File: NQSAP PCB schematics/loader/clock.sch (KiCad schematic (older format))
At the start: 17 parts, among them SW2 PULSE, SW3 RUN, U5 74HCT04, U6 74HCT08, U7 NE556, U8 74HCT27

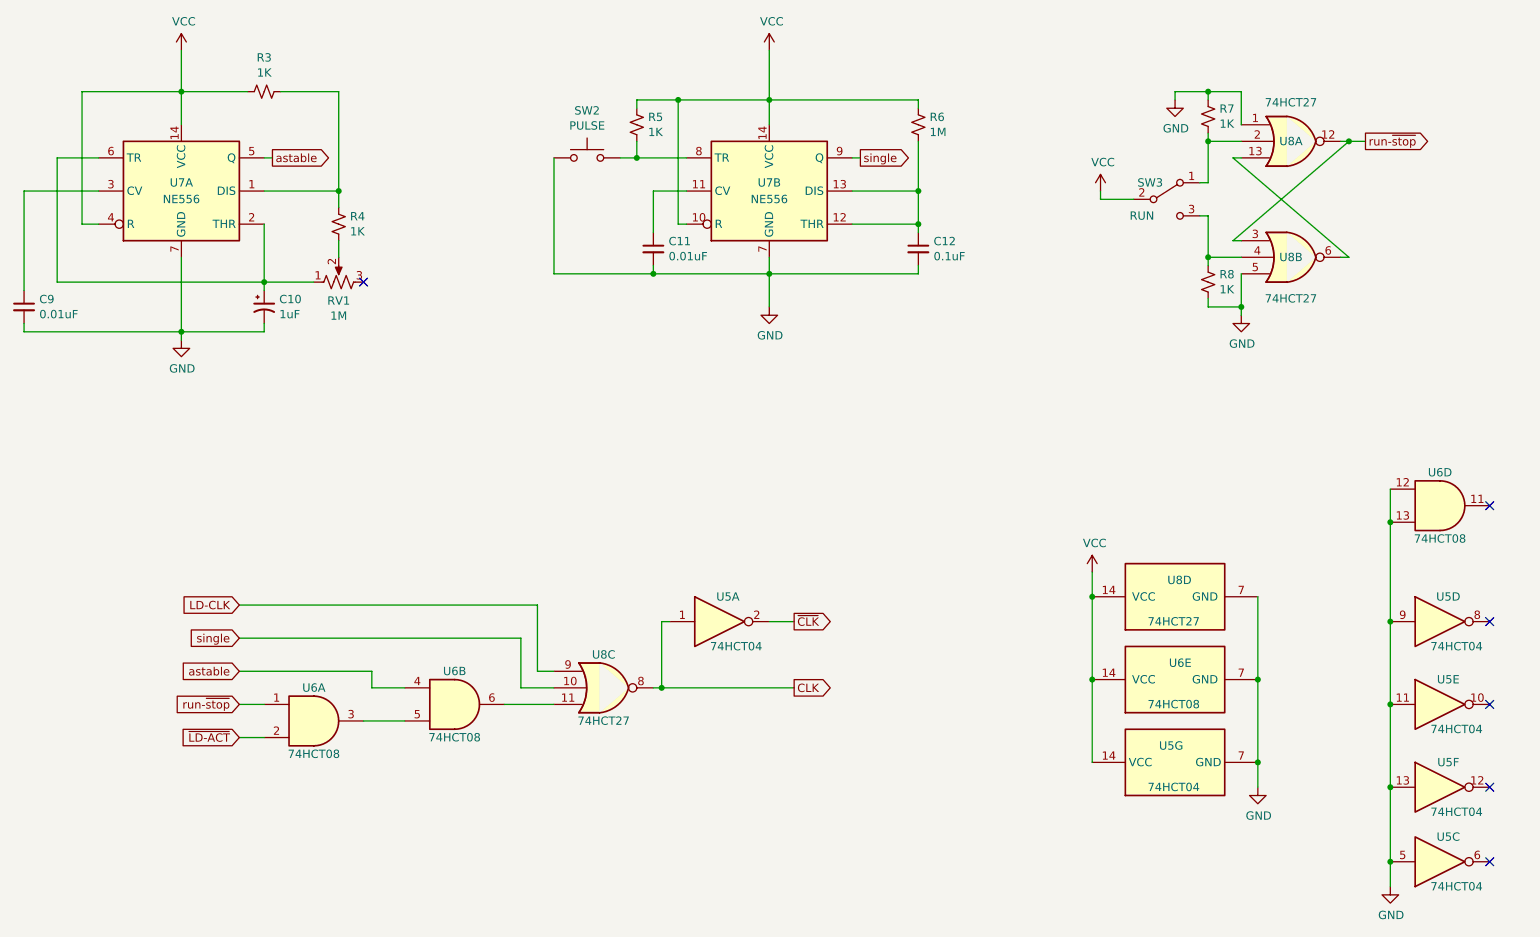
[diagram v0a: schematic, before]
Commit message: Add RAM, update and add gerbers for new boards
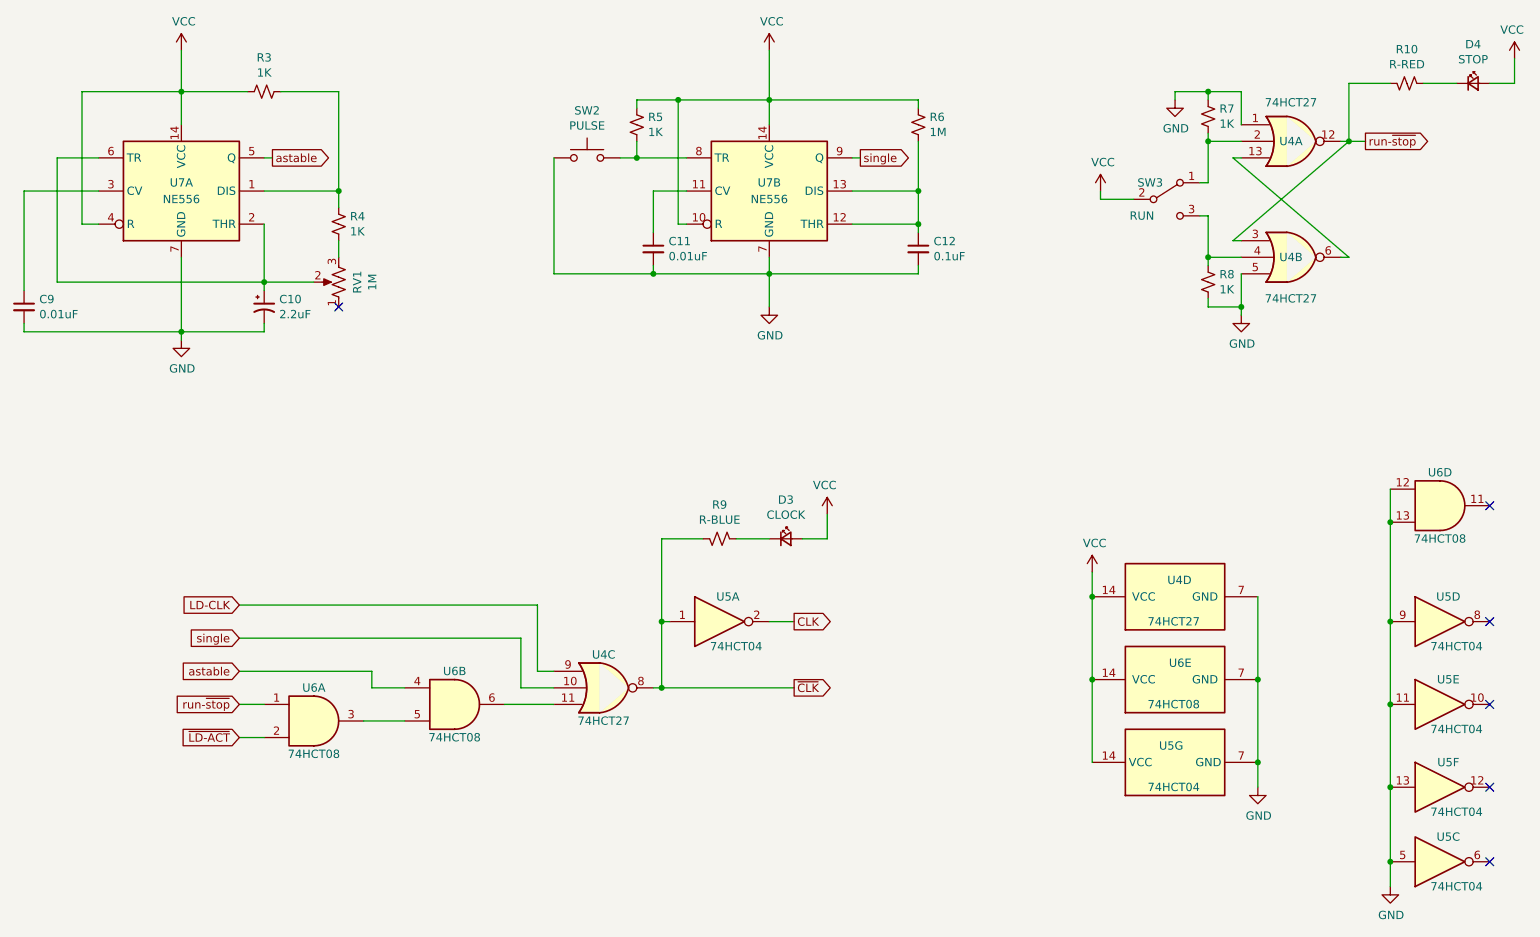
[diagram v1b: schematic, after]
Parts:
- added D3: CLOCK, LED_SMD:LED_0805_2012Metric_Pad1.15x1.40mm_HandSolder, symbol Device:LED_Small
- added D4: STOP, LED_SMD:LED_0805_2012Metric_Pad1.15x1.40mm_HandSolder, symbol Device:LED_Small
- added R10: R-RED, Resistor_SMD:R_0805_2012Metric_Pad1.20x1.40mm_HandSolder, symbol Device:R_Small_US
- added R9: R-BLUE, Resistor_SMD:R_0805_2012Metric_Pad1.20x1.40mm_HandSolder, symbol Device:R_Small_US
- C10: value 1uF -> 2.2uF
- RV1: footprint Potentiometer_THT:Potentiometer_Vishay_T73YP_Vertical -> Potentiometer_THT:Potentiometer_Bourns_3386F_Vertical
- renumbered U8 to U4
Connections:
- net CLK: now also U5.2; no longer U4.8, U5.1
- net VCC: now also D3.2 (A), D4.2 (A)
- net run-~stop: now also R10.1
- net ~CLK: now also U4.8, U5.1, R9.1; no longer U5.2
- net at C10.1, U7.2 (THR), U7.6 (TR): now also RV1.2; no longer RV1.1
- net at R4.1: now also RV1.3; no longer RV1.2
- new net: D4.1 (K), R10.2
- new net: D3.1 (K), R9.2
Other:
- moved on the sheet: RV1
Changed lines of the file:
@@
 $EndComp
 $Comp
-L 74xx:74LS27 U8
+L 74xx:74LS27 U4
 U 1 1 616763BD
 P 8600 1800
-F 0 "U8" H 8600 1800 50  0000 C CNN
+F 0 "U4" H 8600 1800 50  0000 C CNN
 F 1 "74HCT27" H 8600 2034 50  0000 C CNN
 F 2 "Package_DIP:DIP-14_W7.62mm" H 8600 1800 50  0001 C CNN
@@
 $EndComp
 $Comp
-L 74xx:74LS27 U8
+L 74xx:74LS27 U4
 U 2 1 616775EF
 P 8600 2500
-F 0 "U8" H 8600 2500 50  0000 C CNN
+F 0 "U4" H 8600 2500 50  0000 C CNN
 F 1 "74HCT27" H 8600 2250 50  0000 C CNN
 F 2 "Package_DIP:DIP-14_W7.62mm" H 8600 2500 50  0001 C CNN
@@
 $EndComp
 $Comp
-L 74xx:74LS27 U8
+L 74xx:74LS27 U4
 U 3 1 6167911B
 P 4450 5100
-F 0 "U8" H 4450 5300 50  0000 C CNN
+F 0 "U4" H 4450 5300 50  0000 C CNN
 F 1 "74HCT27" H 4450 4900 50  0000 C CNN
 F 2 "Package_DIP:DIP-14_W7.62mm" H 4450 5100 50  0001 C CNN
@@
 $EndComp
 $Comp
-L 74xx:74LS27 U8
+L 74xx:74LS27 U4
 U 4 1 6167A894
 P 7900 4550
-F 0 "U8" V 8000 4450 50  0000 L CNN
+F 0 "U4" V 8000 4450 50  0000 L CNN
 F 1 "74HCT27" V 7750 4400 50  0000 L CNN
 F 2 "Package_DIP:DIP-14_W7.62mm" H 7900 4550 50  0001 C CNN
@@
 F 0 "RV1" V 2737 2650 50  0000 C CNN
 F 1 "1M" V 2646 2650 50  0000 C CNN
-F 2 "Potentiometer_THT:Potentiometer_Vishay_T73YP_Vertical" H 2850 2650 50  0001 C CNN
+F 2 "Potentiometer_THT:Potentiometer_Bourns_3386F_Vertical" H 2850 2650 50  0001 C CNN
 F 3 "~" H 2850 2650 50  0001 C CNN
 	1    2850 2650
-	0    -1   -1   0
+	-1   0    0    1
 $EndComp
 $Comp
@@
 P 2400 2800
 F 0 "C10" H 2491 2846 50  0000 L CNN
-F 1 "1uF" H 2491 2755 50  0000 L CNN
+F 1 "2.2uF" H 2491 2755 50  0000 L CNN
 F 2 "Capacitor_SMD:C_0805_2012Metric_Pad1.18x1.45mm_HandSolder" H 2400 2800 50  0001 C CNN
 F 3 "~" H 2400 2800 50  0001 C CNN
@@
 run-~stop
 Text GLabel 5600 4700 2    50   Output ~ 0
+CLK
+Text GLabel 5600 5100 2    50   Output ~ 0
 ~CLK
-Text GLabel 5600 5100 2    50   Output ~ 0
-CLK
 Wire Wire Line
 	5600 4700 5450 4700
@@
 Wire Wire Line
 	2400 5400 2250 5400
-NoConn ~ 3000 2650
+NoConn ~ 2850 2800
 $Comp
 L 74xx:74HCT04 U5
@@
 Wire Wire Line
 	7400 4550 7400 5050
+$Comp
+L Device:LED_Small D?
+U 1 1 6170AC27
+P 9700 1450
+AR Path="/6170AC27" Ref="D?"  Part="1"
+AR Path="/6164BBEC/6170AC27" Ref="D4"  Part="1"
+F 0 "D4" H 9700 1685 50  0000 C CNN
+F 1 "STOP" H 9700 1594 50  0000 C CNN
+F 2 "LED_SMD:LED_0805_2012Metric_Pad1.15x1.40mm_HandSolder" V 9700 1450 50  0001 C CNN
+F 3 "~" V 9700 1450 50  0001 C CNN
+	1    9700 1450
+	1    0    0    -1
+$EndComp
+$Comp
+L Device:R_Small_US R?
+U 1 1 6170AC2D
+P 9300 1450
+AR Path="/6170AC2D" Ref="R?"  Part="1"
+AR Path="/6164BBEC/6170AC2D" Ref="R10"  Part="1"
+F 0 "R10" V 9095 1450 50  0000 C CNN
+F 1 "R-RED" V 9186 1450 50  0000 C CNN
+F 2 "Resistor_SMD:R_0805_2012Metric_Pad1.20x1.40mm_HandSolder" H 9300 1450 50  0001 C CNN
+F 3 "~" H 9300 1450 50  0001 C CNN
+	1    9300 1450
+	0    -1   1    0
+$EndComp
+Wire Wire Line
+	9600 1450 9400 1450
+Wire Wire Line
+	9200 1450 8950 1450
+Wire Wire Line
+	9800 1450 9950 1450
+Wire Wire Line
+	9950 1300 9950 1450
+$Comp
+L power:VCC #PWR?
+U 1 1 6170AC37
+P 9950 1300
+AR Path="/6170AC37" Ref="#PWR?"  Part="1"
+AR Path="/6164BBEC/6170AC37" Ref="#PWR04"  Part="1"
+F 0 "#PWR04" H 9950 1150 50  0001 C CNN
+F 1 "VCC" H 9965 1473 50  0000 C CNN
+F 2 "" H 9950 1300 50  0001 C CNN
+F 3 "" H 9950 1300 50  0001 C CNN
+	1    9950 1300
+	-1   0    0    -1
+$EndComp
+$Comp
+L Device:LED_Small D?
+U 1 1 6170DDF5
+P 5550 4200
+AR Path="/6170DDF5" Ref="D?"  Part="1"
+AR Path="/6164BBEC/6170DDF5" Ref="D3"  Part="1"
+F 0 "D3" H 5550 4435 50  0000 C CNN
+F 1 "CLOCK" H 5550 4344 50  0000 C CNN
+F 2 "LED_SMD:LED_0805_2012Metric_Pad1.15x1.40mm_HandSolder" V 5550 4200 50  0001 C CNN
+F 3 "~" V 5550 4200 50  0001 C CNN
+	1    5550 4200
+	1    0    0    -1
+$EndComp
+$Comp
+L Device:R_Small_US R?
+U 1 1 6170E577
+P 5150 4200
+AR Path="/6170E577" Ref="R?"  Part="1"
+AR Path="/6164BBEC/6170E577" Ref="R9"  Part="1"
+F 0 "R9" V 4945 4200 50  0000 C CNN
+F 1 "R-BLUE" V 5036 4200 50  0000 C CNN
+F 2 "Resistor_SMD:R_0805_2012Metric_Pad1.20x1.40mm_HandSolder" H 5150 4200 50  0001 C CNN
+F 3 "~" H 5150 4200 50  0001 C CNN
+	1    5150 4200
+	0    -1   1    0
+$EndComp
+Wire Wire Line
+	5450 4200 5250 4200
+Wire Wire Line
+	5050 4200 4800 4200
+Wire Wire Line
+	5650 4200 5800 4200
+Wire Wire Line
+	5800 4050 5800 4200
+$Comp
+L power:VCC #PWR?
+U 1 1 6170E585
+P 5800 4050
+AR Path="/6170E585" Ref="#PWR?"  Part="1"
+AR Path="/6164BBEC/6170E585" Ref="#PWR03"  Part="1"
+F 0 "#PWR03" H 5800 3900 50  0001 C CNN
+F 1 "VCC" H 5815 4223 50  0000 C CNN
+F 2 "" H 5800 4050 50  0001 C CNN
+F 3 "" H 5800 4050 50  0001 C CNN
+	1    5800 4050
+	-1   0    0    -1
+$EndComp
+Wire Wire Line
+	4800 4200 4800 4700
+Connection ~ 4800 4700
+Wire Wire Line
+	8950 1450 8950 1800
 $EndSCHEMATC

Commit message: build 5 board updates
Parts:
- added J4: CLK Select, Connector_PinHeader_2.54mm:PinHeader_1x03_P2.54mm_Vertical, symbol Connector_Generic:Conn_01x03
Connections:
- net GND: now also J4.3 (Pin_3)
- net astable: now also J4.1 (Pin_1); no longer U6.4
- new net: J4.2 (Pin_2), U6.4
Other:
- note added: "Jumper pins 1 and 2 for\ninternal clock or inject\nexternal clock on pins 2 and 3."
- moved on the sheet: D3, R9, U4C, U5A, U6A, U6B
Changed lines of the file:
@@
 L 74xx:74HCT04 U5
 U 1 1 616651FA
-P 5150 4700
-F 0 "U5" H 5200 4850 50  0000 C CNN
-F 1 "74HCT04" H 5250 4550 50  0000 C CNN
-F 2 "Package_DIP:DIP-14_W7.62mm" H 5150 4700 50  0001 C CNN
-F 3 "https://assets.nexperia.com/documents/data-sheet/74HC_HCT04.pdf" H 5150 4700 50  0001 C CNN
-	1    5150 4700
+P 5700 5050
+F 0 "U5" H 5750 5200 50  0000 C CNN
+F 1 "74HCT04" H 5800 4900 50  0000 C CNN
+F 2 "Package_DIP:DIP-14_W7.62mm" H 5700 5050 50  0001 C CNN
+F 3 "https://assets.nexperia.com/documents/data-sheet/74HC_HCT04.pdf" H 5700 5050 50  0001 C CNN
+	1    5700 5050
 	1    0    0    -1
 $EndComp
@@
 L 74xx:74LS08 U6
 U 1 1 6166BA07
-P 2700 5300
-F 0 "U6" H 2700 5500 50  0000 C CNN
-F 1 "74HCT08" H 2700 5100 50  0000 C CNN
-F 2 "Package_DIP:DIP-14_W7.62mm" H 2700 5300 50  0001 C CNN
-F 3 "http://www.ti.com/lit/gpn/sn74LS08" H 2700 5300 50  0001 C CNN
-	1    2700 5300
+P 3250 5650
+F 0 "U6" H 3250 5850 50  0000 C CNN
+F 1 "74HCT08" H 3250 5450 50  0000 C CNN
+F 2 "Package_DIP:DIP-14_W7.62mm" H 3250 5650 50  0001 C CNN
+F 3 "http://www.ti.com/lit/gpn/sn74LS08" H 3250 5650 50  0001 C CNN
+	1    3250 5650
 	1    0    0    -1
 $EndComp
@@
 L 74xx:74LS08 U6
 U 2 1 6166C808
-P 3550 5200
-F 0 "U6" H 3550 5400 50  0000 C CNN
-F 1 "74HCT08" H 3550 5000 50  0000 C CNN
-F 2 "Package_DIP:DIP-14_W7.62mm" H 3550 5200 50  0001 C CNN
-F 3 "http://www.ti.com/lit/gpn/sn74LS08" H 3550 5200 50  0001 C CNN
-	2    3550 5200
+P 4100 5550
+F 0 "U6" H 4100 5750 50  0000 C CNN
+F 1 "74HCT08" H 4100 5350 50  0000 C CNN
+F 2 "Package_DIP:DIP-14_W7.62mm" H 4100 5550 50  0001 C CNN
+F 3 "http://www.ti.com/lit/gpn/sn74LS08" H 4100 5550 50  0001 C CNN
+	2    4100 5550
 	1    0    0    -1
 $EndComp
@@
 L 74xx:74LS27 U4
 U 3 1 6167911B
-P 4450 5100
-F 0 "U4" H 4450 5300 50  0000 C CNN
-F 1 "74HCT27" H 4450 4900 50  0000 C CNN
-F 2 "Package_DIP:DIP-14_W7.62mm" H 4450 5100 50  0001 C CNN
-F 3 "http://www.ti.com/lit/gpn/sn74LS27" H 4450 5100 50  0001 C CNN
-	3    4450 5100
+P 5000 5450
+F 0 "U4" H 5000 5650 50  0000 C CNN
+F 1 "74HCT27" H 5000 5250 50  0000 C CNN
+F 2 "Package_DIP:DIP-14_W7.62mm" H 5000 5450 50  0001 C CNN
+F 3 "http://www.ti.com/lit/gpn/sn74LS27" H 5000 5450 50  0001 C CNN
+	3    5000 5450
 	1    0    0    -1
 $EndComp
@@
 Text GLabel 9050 1800 2    50   Output ~ 0
 run-~stop
-Text GLabel 2250 5200 0    50   Input ~ 0
+Text GLabel 2800 5550 0    50   Input ~ 0
 run-~stop
-Text GLabel 5600 4700 2    50   Output ~ 0
+Text GLabel 6150 5050 2    50   Output ~ 0
 CLK
-Text GLabel 5600 5100 2    50   Output ~ 0
+Text GLabel 6150 5450 2    50   Output ~ 0
 ~CLK
 Wire Wire Line
-	5600 4700 5450 4700
-Wire Wire Line
-	5600 5100 4800 5100
-Wire Wire Line
-	4850 4700 4800 4700
-Wire Wire Line
-	4800 4700 4800 5100
-Connection ~ 4800 5100
-Wire Wire Line
-	4800 5100 4750 5100
-Wire Wire Line
-	4150 5200 3850 5200
-Wire Wire Line
-	3250 5300 3000 5300
-Wire Wire Line
-	2400 5200 2250 5200
-Text GLabel 2250 4800 0    50   Input ~ 0
+	6150 5050 6000 5050
+Wire Wire Line
+	6150 5450 5350 5450
+Wire Wire Line
+	5400 5050 5350 5050
+Wire Wire Line
+	5350 5050 5350 5450
+Connection ~ 5350 5450
+Wire Wire Line
+	5350 5450 5300 5450
+Wire Wire Line
+	4700 5550 4400 5550
+Wire Wire Line
+	3800 5650 3550 5650
+Wire Wire Line
+	2950 5550 2800 5550
+Text GLabel 2800 5150 0    50   Input ~ 0
 single
-Text GLabel 2250 5000 0    50   Input ~ 0
+Text GLabel 1850 4750 0    50   Input ~ 0
 astable
 Wire Wire Line
-	2250 5000 3050 5000
-Wire Wire Line
-	3050 5000 3050 5100
-Wire Wire Line
-	3050 5100 3250 5100
-Wire Wire Line
-	2250 4800 3950 4800
-Wire Wire Line
-	3950 4800 3950 5100
-Wire Wire Line
-	3950 5100 4150 5100
-Wire Wire Line
-	4150 5000 4050 5000
-Wire Wire Line
-	4050 5000 4050 4600
-Wire Wire Line
-	4050 4600 2250 4600
+	1850 5350 3600 5350
+Wire Wire Line
+	3600 5350 3600 5450
+Wire Wire Line
+	3600 5450 3800 5450
+Wire Wire Line
+	2800 5150 4500 5150
+Wire Wire Line
+	4500 5150 4500 5450
+Wire Wire Line
+	4500 5450 4700 5450
+Wire Wire Line
+	4700 5350 4600 5350
+Wire Wire Line
+	4600 5350 4600 4950
+Wire Wire Line
+	4600 4950 2800 4950
 NoConn ~ 9800 4000
 NoConn ~ 9800 4700
@@
 Wire Wire Line
 	8400 5550 8400 5700
-Text GLabel 2250 4600 0    50   Input ~ 0
+Text GLabel 2800 4950 0    50   Input ~ 0
 LD-CLK
-Text GLabel 2250 5400 0    50   Input ~ 0
+Text GLabel 2800 5750 0    50   Input ~ 0
 ~LD-ACT
 Wire Wire Line
-	2400 5400 2250 5400
+	2950 5750 2800 5750
 NoConn ~ 2850 2800
 $Comp
@@
 L Device:LED_Small D?
 U 1 1 6170DDF5
-P 5550 4200
+P 6100 4550
 AR Path="/6170DDF5" Ref="D?"  Part="1"
 AR Path="/6164BBEC/6170DDF5" Ref="D3"  Part="1"
-F 0 "D3" H 5550 4435 50  0000 C CNN
-F 1 "CLOCK" H 5550 4344 50  0000 C CNN
-F 2 "LED_SMD:LED_0805_2012Metric_Pad1.15x1.40mm_HandSolder" V 5550 4200 50  0001 C CNN
-F 3 "~" V 5550 4200 50  0001 C CNN
-	1    5550 4200
+F 0 "D3" H 6100 4785 50  0000 C CNN
+F 1 "CLOCK" H 6100 4694 50  0000 C CNN
+F 2 "LED_SMD:LED_0805_2012Metric_Pad1.15x1.40mm_HandSolder" V 6100 4550 50  0001 C CNN
+F 3 "~" V 6100 4550 50  0001 C CNN
+	1    6100 4550
 	1    0    0    -1
 $EndComp
@@
 L Device:R_Small_US R?
 U 1 1 6170E577
-P 5150 4200
+P 5700 4550
 AR Path="/6170E577" Ref="R?"  Part="1"
 AR Path="/6164BBEC/6170E577" Ref="R9"  Part="1"
-F 0 "R9" V 4945 4200 50  0000 C CNN
-F 1 "R-BLUE" V 5036 4200 50  0000 C CNN
-F 2 "Resistor_SMD:R_0805_2012Metric_Pad1.20x1.40mm_HandSolder" H 5150 4200 50  0001 C CNN
-F 3 "~" H 5150 4200 50  0001 C CNN
-	1    5150 4200
+F 0 "R9" V 5495 4550 50  0000 C CNN
+F 1 "R-BLUE" V 5586 4550 50  0000 C CNN
+F 2 "Resistor_SMD:R_0805_2012Metric_Pad1.20x1.40mm_HandSolder" H 5700 4550 50  0001 C CNN
+F 3 "~" H 5700 4550 50  0001 C CNN
+	1    5700 4550
 	0    -1   1    0
 $EndComp
 Wire Wire Line
-	5450 4200 5250 4200
-Wire Wire Line
-	5050 4200 4800 4200
-Wire Wire Line
-	5650 4200 5800 4200
-Wire Wire Line
-	5800 4050 5800 4200
+	6000 4550 5800 4550
+Wire Wire Line
+	5600 4550 5350 4550
+Wire Wire Line
+	6200 4550 6350 4550
+Wire Wire Line
+	6350 4400 6350 4550
 $Comp
 L power:VCC #PWR?
 U 1 1 6170E585
-P 5800 4050
+P 6350 4400
 AR Path="/6170E585" Ref="#PWR?"  Part="1"
 AR Path="/6164BBEC/6170E585" Ref="#PWR03"  Part="1"
-F 0 "#PWR03" H 5800 3900 50  0001 C CNN
-F 1 "VCC" H 5815 4223 50  0000 C CNN
-F 2 "" H 5800 4050 50  0001 C CNN
-F 3 "" H 5800 4050 50  0001 C CNN
-	1    5800 4050
+F 0 "#PWR03" H 6350 4250 50  0001 C CNN
+F 1 "VCC" H 6365 4573 50  0000 C CNN
+F 2 "" H 6350 4400 50  0001 C CNN
+F 3 "" H 6350 4400 50  0001 C CNN
+	1    6350 4400
 	-1   0    0    -1
 $EndComp
 Wire Wire Line
-	4800 4200 4800 4700
-Connection ~ 4800 4700
+	5350 4550 5350 5050
+Connection ~ 5350 5050
 Wire Wire Line
 	8950 1450 8950 1800
+$Comp
+L Connector_Generic:Conn_01x03 J4
+U 1 1 630B7A32
+P 1650 5350
+F 0 "J4" H 1568 5667 50  0000 C CNN
+F 1 "CLK Select" H 1568 5576 50  0000 C CNN
+F 2 "Connector_PinHeader_2.54mm:PinHeader_1x03_P2.54mm_Vertical" H 1650 5350 50  0001 C CNN
+F 3 "~" H 1650 5350 50  0001 C CNN
+	1    1650 5350
+	-1   0    0    -1
+$EndComp
+Wire Wire Line
+	1850 4750 2000 4750
+Wire Wire Line
+	2000 4750 2000 5250
+Wire Wire Line
+	2000 5250 1850 5250
+Wire Wire Line
+	1850 5450 1900 5450
+Wire Wire Line
+	1900 5450 1900 5500
+$Comp
+L power:GND #PWR05
+U 1 1 630C4178
+P 1900 5500
+F 0 "#PWR05" H 1900 5250 50  0001 C CNN
+F 1 "GND" H 1905 5327 50  0000 C CNN
+F 2 "" H 1900 5500 50  0001 C CNN
+F 3 "" H 1900 5500 50  0001 C CNN
+	1    1900 5500
+	1    0    0    -1
+$EndComp
+Text Notes 1200 6100 0    50   ~ 0
+Jumper pins 1 and 2 for\ninternal clock or inject\nexternal clock on pins 2 and 3.
 $EndSCHEMATC
